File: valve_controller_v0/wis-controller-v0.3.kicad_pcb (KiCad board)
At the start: 2 copper layers, 78 x 110 mm, 68 parts, among them J11 Solenoid_connector, J3 USB_C_Receptacle_USB2.0, J5 SWD, J6 JST-2PH, Q1 DMG3415UQ-7, SW1 RESET, SW3 SW_DIP_x02, SW4 BOOT, U1 RAK3172, U10 BAT_Positive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

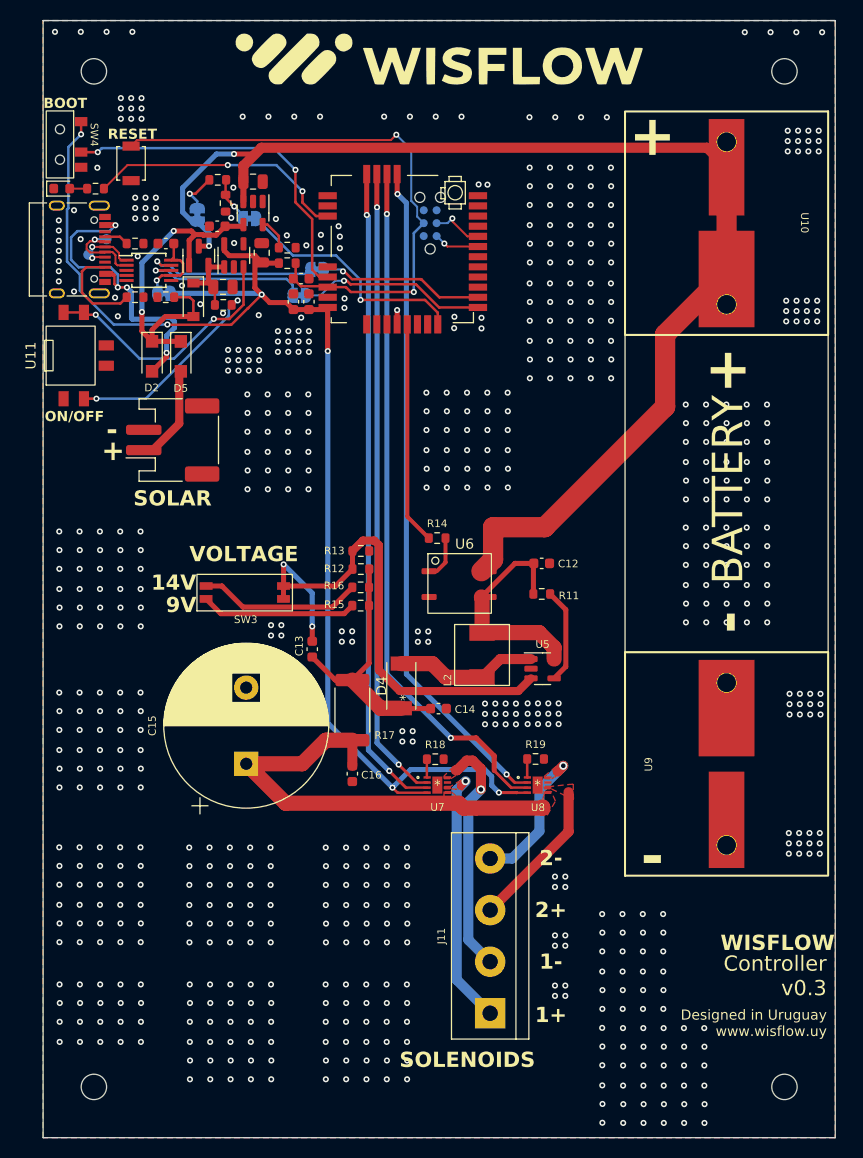
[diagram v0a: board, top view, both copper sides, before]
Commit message: Replaced battery charger and battery holder
- Replaced battery charger to support the  new solar panel
- Replaced the battery holder by a plastic enclosure one
- Reconnected the on/off switch to avoid putting EN pin floating temporarly whne swithced
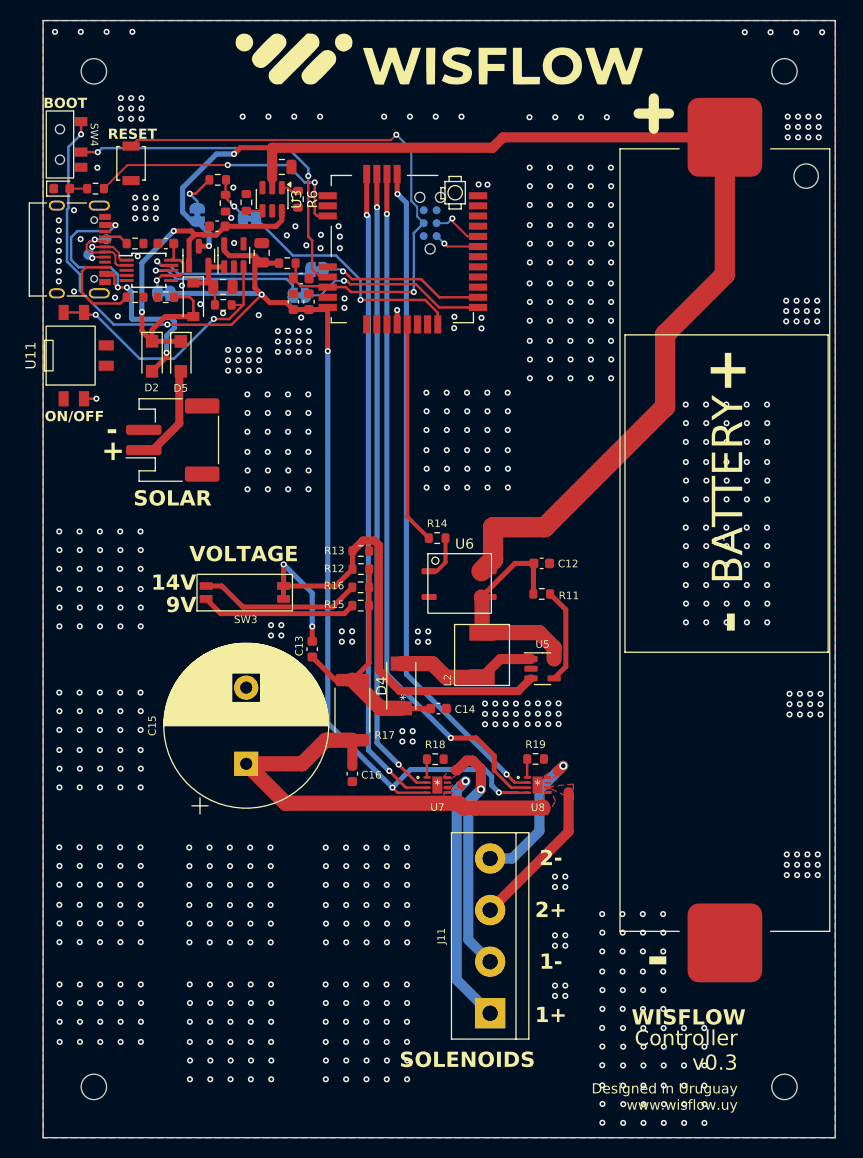
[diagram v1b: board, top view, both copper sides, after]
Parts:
- removed U10: BAT_Positive, WIS_Solenoid_Power_module:Battery_holder_18650
- removed U9: BAT_Negative, WIS_Solenoid_Power_module:Battery_holder_18650
- added J1: 18650 Socket, Wisflow:18650_SMD, F.Cu at (167.1, 71.2)
- added R6: 10K, Resistor_SMD:R_0603_1608Metric, F.Cu at (125.1, 37.6)
- R5: value 5.1K -> 2.7k
- U11: value ~ -> XKB5858-Z-F-75
- U3: value MCP73831T-2ACI/OT -> BQ21040DBV; footprint Package_TO_SOT_SMD:SOT-23-5 -> Package_TO_SOT_SMD:SOT-23-6
- moved R5 6.01 mm to (120.0, 37.9), turned to 90 degrees
- moved C8 3.18 mm to (123.5, 34.4)
- moved U3 2.32 mm to (122.6, 37.6)
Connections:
- R5 pad 1: Net-(U3-PROG) -> Net-(U3-ISET)
- R8 pad 1: Net-(R8-Pad1) -> /EN
- U11 pad 2: Net-(R8-Pad1) -> unconnected-(U11-Pad2)
- U3 pad 1: unconnected-(U3-STAT-Pad1) -> Net-(U3-TS)
- U3 pad 2: GND -> +BATT
- U3 pad 3: +BATT -> unconnected-(U3-~{CHG}-Pad3)
- U3 pad 4: VBUS_D -> Net-(U3-ISET)
- U3 pad 5: Net-(U3-PROG) -> GND
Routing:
- net Net-(R8-Pad1): track 20.3 -> 0.00 mm, vias 2 -> 0
- net VBUS_D: track 35.5 -> 40.4 mm
- net Net-(U3-PROG): track 3.21 -> 0.00 mm
- net Net-(U3-TS): track 0.00 -> 1.72 mm
- net Net-(U3-ISET): track 0.00 -> 1.59 mm
- net unconnected-(U11-Pad2): track 0.00 -> 1.23 mm, vias 0 -> 1
- net /EN: track 25.5 -> 26.7 mm
- net /PA8: track 25.7 -> 26.9 mm
- net +BATT: track 123.3 -> 122.2 mm
- net Net-(SW4A-B): track 34.5 -> 35.3 mm

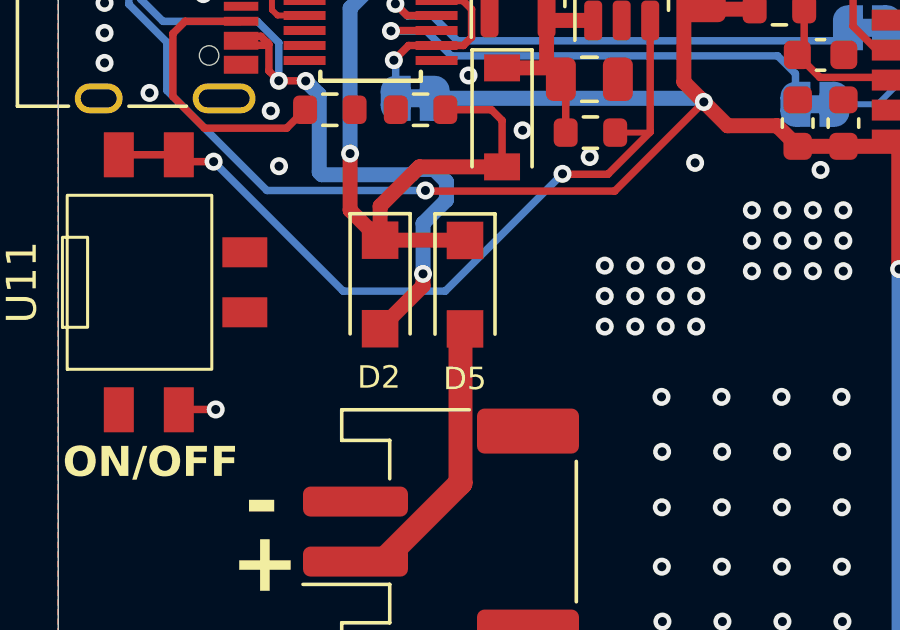
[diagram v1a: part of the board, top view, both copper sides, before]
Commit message: Uniformized D2,D3 and D5
- Selected the same partnumber forD2, D3 and D5, all of the 1A and 40V.
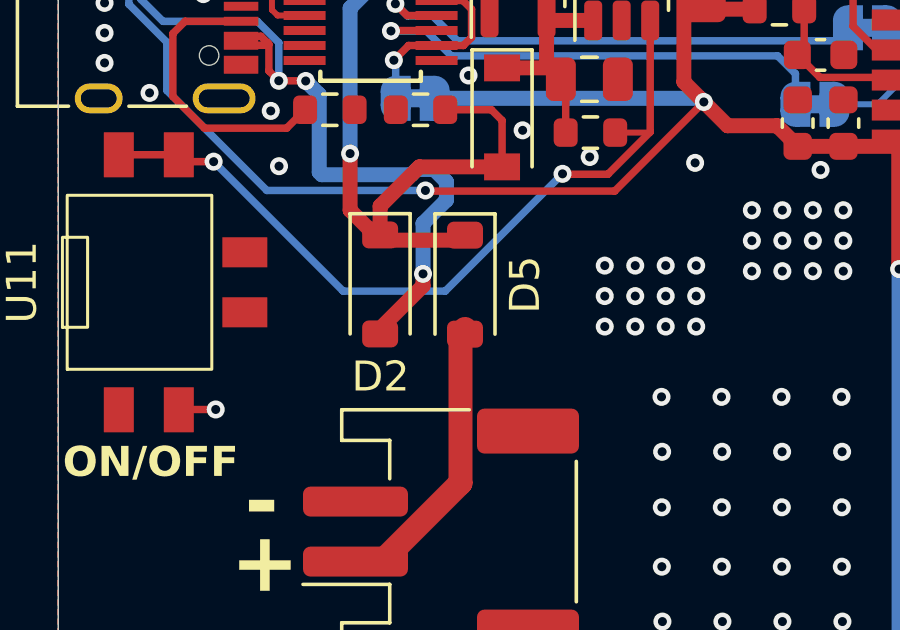
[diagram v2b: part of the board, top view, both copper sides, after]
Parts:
- D2, D5: value MBR140SFT1G -> B5819W; footprint WIS_Solenoid_Power_module:D_MBR140SF -> Diode_SMD:D_SOD-123
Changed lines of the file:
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@@
 		)
 	)
-	(footprint "WIS_Solenoid_Power_module:D_MBR140SF"
+	(footprint "Diode_SMD:D_SOD-123"
 		(layer "F.Cu")
 		(at 113.56 53.07 -90)
@@
 		(tags "SOD-123")
 		(property "Reference" "D5"
-			(at 3.135 0.005 180)
+			(at 0 -2 270)
 			(layer "F.SilkS")
 			(effects
 				(font
-					(size 0.75 0.75)
-					(thickness 0.125)
+					(size 1 1)
+					(thickness 0.15)
 				)
 			)
 		)
-		(property "Value" "MBR140SFT1G"
-			(at 0 2.1 90)
+		(property "Value" "B5819W"
+			(at 0 2.1 270)
 			(layer "F.Fab")
-			(hide yes)
 			(effects
 				(font
-					(size 0.75 0.75)
-					(thickness 0.125)
+					(size 1 1)
+					(thickness 0.15)
 				)
 			)
@@
 		(property "Datasheet" "~"
 			(at 0 0 270)
+			(unlocked yes)
 			(layer "F.Fab")
 			(hide yes)
@@
 		(property "Description" ""
 			(at 0 0 270)
+			(unlocked yes)
 			(layer "F.Fab")
 			(hide yes)
@@
 			(layer "F.Fab")
 		)
-		(pad "1" smd rect
-			(at -1.475 0 270)
-			(size 1.25 1.22)
+		(fp_text user "${REFERENCE}"
+			(at 0 -2 270)
+			(layer "F.Fab")
+			(effects
+				(font
+					(size 1 1)
+					(thickness 0.15)
+				)
+			)
+		)
+		(pad "1" smd roundrect
+			(at -1.65 0 270)
+			(size 0.9 1.2)
 			(layers "F.Cu" "F.Mask" "F.Paste")
+			(roundrect_rratio 0.25)
 			(net 35 "VBUS_D")
 			(pinfunction "K")
 			(pintype "passive")
 		)
-		(pad "2" smd rect
-			(at 1.475 0 270)
-			(size 1.25 1.22)
+		(pad "2" smd roundrect
+			(at 1.65 0 270)
+			(size 0.9 1.2)
 			(layers "F.Cu" "F.Mask" "F.Paste")
+			(roundrect_rratio 0.25)
 			(net 36 "/V_SOLAR")
 			(pinfunction "A")
@@
 		)
 		(embedded_fonts no)
-		(model "${KICAD6_3DMODEL_DIR}/Diode_SMD.3dshapes/D_SOD-123.wrl"
+		(model "${KICAD9_3DMODEL_DIR}/Diode_SMD.3dshapes/D_SOD-123.step"
 			(offset
 				(xyz 0 0 0)
@@
 		)
 		(property "Value" "B5819W"
-			(at 2.794 0.0508 180)
+			(at 2.794 0.0508 0)
 			(layer "F.Fab")
 			(hide yes)
@@
 		)
 		(property "Datasheet" ""
-			(at 0 0 270)
+			(at 0 0 90)
 			(layer "F.Fab")
 			(hide yes)
@@
 		)
 		(property "Description" ""
-			(at 0 0 270)
+			(at 0 0 90)
 			(layer "F.Fab")
 			(hide yes)
@@
 		)
 		(fp_text user "${REFERENCE}"
-			(at 2.8016 0.0166 180)
+			(at 2.8016 0.0166 0)
 			(layer "F.Fab")
 			(effects
@@
 		)
 	)
-	(footprint "WIS_Solenoid_Power_module:D_MBR140SF"
+	(footprint "Diode_SMD:D_SOD-123"
 		(layer "F.Cu")
 		(at 110.73 53.0625 -90)
@@
 		(tags "SOD-123")
 		(property "Reference" "D2"
-			(at 3.095 0.04 180)
+			(at 3.0715 -0.014 180)
 			(layer "F.SilkS")
 			(effects
 				(font
-					(size 0.75 0.75)
-					(thickness 0.125)
+					(size 1 1)
+					(thickness 0.15)
 				)
 			)
 		)
-		(property "Value" "MBR140SFT1G"
+		(property "Value" "B5819W"
 			(at 0 2.1 90)
 			(layer "F.Fab")
-			(hide yes)
 			(effects
 				(font
-					(size 0.75 0.75)
-					(thickness 0.125)
+					(size 1 1)
+					(thickness 0.15)
 				)
 			)
@@
 		(property "Datasheet" "~"
 			(at 0 0 270)
+			(unlocked yes)
 			(layer "F.Fab")
 			(hide yes)
@@
 		(property "Description" ""
 			(at 0 0 270)
+			(unlocked yes)
 			(layer "F.Fab")
 			(hide yes)
@@
 			(layer "F.Fab")
 		)
-		(pad "1" smd rect
-			(at -1.475 0 270)
-			(size 1.25 1.22)
+		(fp_text user "${REFERENCE}"
+			(at 0 -2 90)
+			(layer "F.Fab")
+			(effects
+				(font
+					(size 1 1)
+					(thickness 0.15)
+				)
+			)
+		)
+		(pad "1" smd roundrect
+			(at -1.65 0 270)
+			(size 0.9 1.2)
 			(layers "F.Cu" "F.Mask" "F.Paste")
+			(roundrect_rratio 0.25)
 			(net 35 "VBUS_D")
 			(pinfunction "K")
 			(pintype "passive")
 		)
-		(pad "2" smd rect
-			(at 1.475 0 270)
-			(size 1.25 1.22)
+		(pad "2" smd roundrect
+			(at 1.65 0 270)
+			(size 0.9 1.2)
 			(layers "F.Cu" "F.Mask" "F.Paste")
+			(roundrect_rratio 0.25)
 			(net 9 "VBUS")
 			(pinfunction "A")
@@
 		)
 		(embedded_fonts no)
-		(model "${KICAD6_3DMODEL_DIR}/Diode_SMD.3dshapes/D_SOD-123.wrl"
+		(model "${KICAD9_3DMODEL_DIR}/Diode_SMD.3dshapes/D_SOD-123.step"
 			(offset
 				(xyz 0 0 0)
